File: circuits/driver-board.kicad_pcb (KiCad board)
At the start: 4 copper layers, 40 x 47 mm, 74 parts, among them J1 Conn_01x18_Female, J2 USB4120-03-C_REVA, J3 Motor_Conn_01x04, J4 Screw_Terminals, J5 Conn_01x06_Female, Q1 SS8050-G, Q2 SS8050-G, SW1 RST_SW_Push, U1 CP2102N-Axx-xQFN24, U2 BA33DD0T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

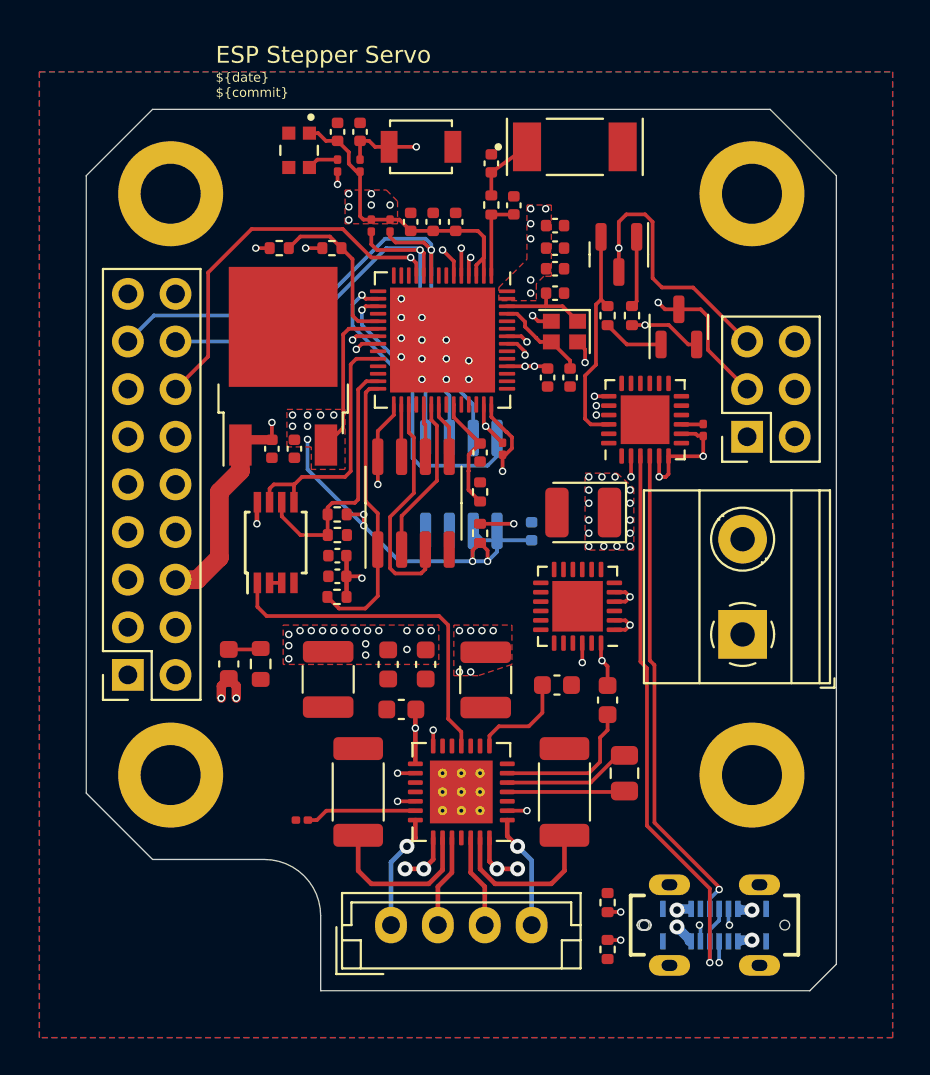
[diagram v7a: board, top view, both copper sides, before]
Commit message: first finished tracing; missing expboard connections and bom
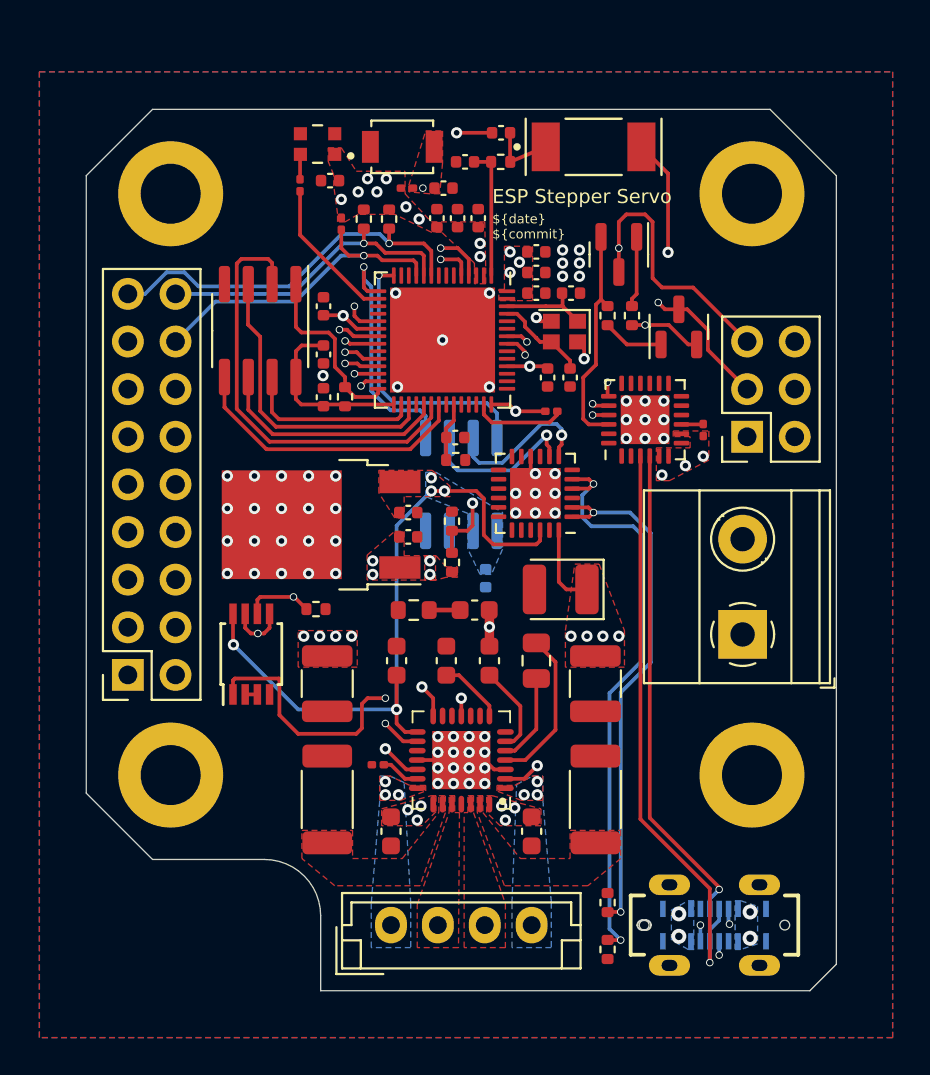
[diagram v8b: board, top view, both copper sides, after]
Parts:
- removed R2: 20K, Resistor_SMD:R_0402_1005Metric
- added C17: 100nF, Capacitor_SMD:C_0402_1005Metric, F.Cu at (54.0, 39.8)
- C5: value 1µF -> 10µF
- C7: value 10nF -> 1µF
- R20, R21: footprint Resistor_SMD:R_0201_0603Metric -> Resistor_SMD:R_0402_1005Metric
- R7: footprint Resistor_SMD:R_0402_1005Metric -> Resistor_SMD:R_0201_0603Metric
- U5: footprint Package_DFN_QFN:QFN-28-1EP_5x5mm_P0.5mm_EP3.35x3.35mm_ThermalVias -> trinamic-footprints:QFN28P
- moved R5 19.1 mm to (49.5, 54.2), turned to 90 degrees
- moved R7 18.1 mm to (43.6, 36.1), turned to 90 degrees
- moved R6 15.9 mm to (49.5, 52.0), turned to 90 degrees
- moved C8 13.4 mm to (50.7, 56.7), turned to 180 degrees
- moved C32 13.1 mm to (42.6, 40.5), turned to -90 degrees
- moved U7 12.3 mm to (39.3, 41.8), turned to -90 degrees
- moved C29 10.8 mm to (42.6, 43.1), turned to 90 degrees
- moved R9 10.7 mm to (43.8, 45.3), turned to 90 degrees
- moved C13 10.5 mm to (53.8, 68.5)
- moved C28 9.58 mm to (42.6, 45.4), turned to -90 degrees
- moved C12 8.90 mm to (46.2, 68.5)
- moved U2 8.69 mm to (42.5, 52.1), turned to 180 degrees
- moved C3 8.66 mm to (47.2, 52.8), turned to 180 degrees
- moved R3 8.65 mm to (47.5, 56.7), turned to 180 degrees
- moved C11 7.62 mm to (54.0, 59.4), turned to 90 degrees
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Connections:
- net /ESP_IO14 renamed /VBUS_SENSE / ESP_IO14
- net Net-(AE1-Pad1) renamed /ANTENNA
- net Net-(R12-Pad2) renamed /TMC2209_BRA
- net Net-(R13-Pad2) renamed /TMC2209_BRB
- H1 pad 1: GND -> (no net)
- H2 pad 1: GND -> (no net)
- H3 pad 1: GND -> (no net)
- H4 pad 1: GND -> (no net)
- J1 pad 14: /TMC2209_EN / ESP_IO06 -> unconnected-(J1-Pad14)
- J1 pad 15: /I2C_SCL / ESP_IO04 -> unconnected-(J1-Pad15)
- J1 pad 16: /I2C_SDA / ESP_IO05 -> /TMC2209_EN / ESP_IO06
- J1 pad 17: /UART1_RXD / ESP_IO46 -> /I2C_SCL / ESP_IO04
- J1 pad 18: /UART1_TXD / ESP_IO45 -> /I2C_SDA / ESP_IO05
- R4 pad 1: /LED / ESP_IO01 -> /LED / ESP_IO11
- U3 pad 14: /ESP_IO09 -> /AS5601_A_ITR / ESP_IO09
- U3 pad 15: /ESP_IO10 -> /AS5601_B_ITR / ESP_IO10
- U3 pad 16: /AS5601_A_ITR / ESP_IO11 -> /LED / ESP_IO11
- U3 pad 17: /AS5601_B_ITR / ESP_IO12 -> /ESP_IO12
- U3 pad 6: /LED / ESP_IO01 -> /ESP_IO01
- U4 pad 5: /AS5601_B_ITR / ESP_IO12 -> /AS5601_B_ITR / ESP_IO10
- U4 pad 8: /AS5601_A_ITR / ESP_IO11 -> /AS5601_A_ITR / ESP_IO09
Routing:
- net +3V3: track 84.4 -> 42.4 mm, vias 30 -> 22
- net VBUS: track 60.8 -> 27.7 mm, vias 51 -> 23
- net /UART1_RXD / ESP_IO46: track 48.9 -> 21.6 mm
- net /UART1_TXD / ESP_IO45: track 24.9 -> 4.98 mm, vias 1 -> 0
- net /AS5601_A_ITR / ESP_IO11: track 17.0 -> 0.00 mm, vias 1 -> 0
- net /AS5601_A_ITR / ESP_IO09: track 0.00 -> 15.0 mm, vias 0 -> 1
- net /SPIQ / ESP_IO31: track 8.66 -> 23.3 mm
- net /AS5601_B_ITR / ESP_IO10: track 0.00 -> 13.4 mm, vias 0 -> 1
- net /SR_Q / ESP_IO18: track 13.7 -> 26.3 mm, vias 0 -> 2
- net /SPID / ESP_IO32: track 3.02 -> 15.5 mm
- net /USB_CC2: track 26.9 -> 37.5 mm
- net /VBUS_SENSE / ESP_IO14: track 8.65 -> 18.6 mm, vias 0 -> 2
- net /LED / ESP_IO01: track 9.85 -> 0.00 mm, vias 2 -> 0
- net /SPICLK / ESP_IO30: track 2.82 -> 12.6 mm
- net /USB_CC1: track 27.7 -> 37.0 mm
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- added copper zone on B.Cu, net +3V3
- added copper zone on F.Cu, net /ESP_EN
- added copper zone on F.Cu, net /TMC2209_BRA
- added copper zone on F.Cu, net /TMC2209_BRB
- added copper zone on F.Cu, net /TMC2209_OA1
- added copper zone on B.Cu, net /TMC2209_OA2
- added copper zone on F.Cu, net /TMC2209_OA2
- added copper zone on F.Cu, net /TMC2209_OB1
- added copper zone on B.Cu, net /TMC2209_OB2
- added copper zone on F.Cu, net /TMC2209_OB2
- added copper zone on B.Cu, net VBUS
